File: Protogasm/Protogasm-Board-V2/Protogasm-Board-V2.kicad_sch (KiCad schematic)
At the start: 10 parts, among them J1 Neopixel_Ring_Header, M1 Motor_DC, Q1 FQP30N06L, SW1 Rotary_Encoder_Switch, U1 Arduino_UNO_R3, U2 MPX5050GP

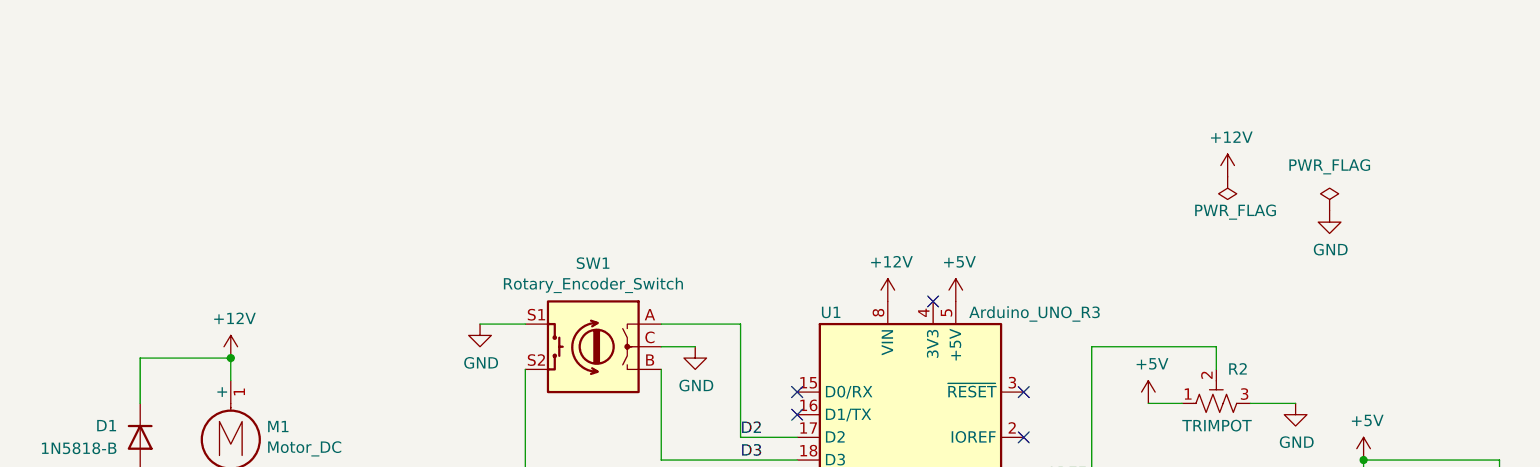
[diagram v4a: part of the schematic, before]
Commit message: Update schematic for V4
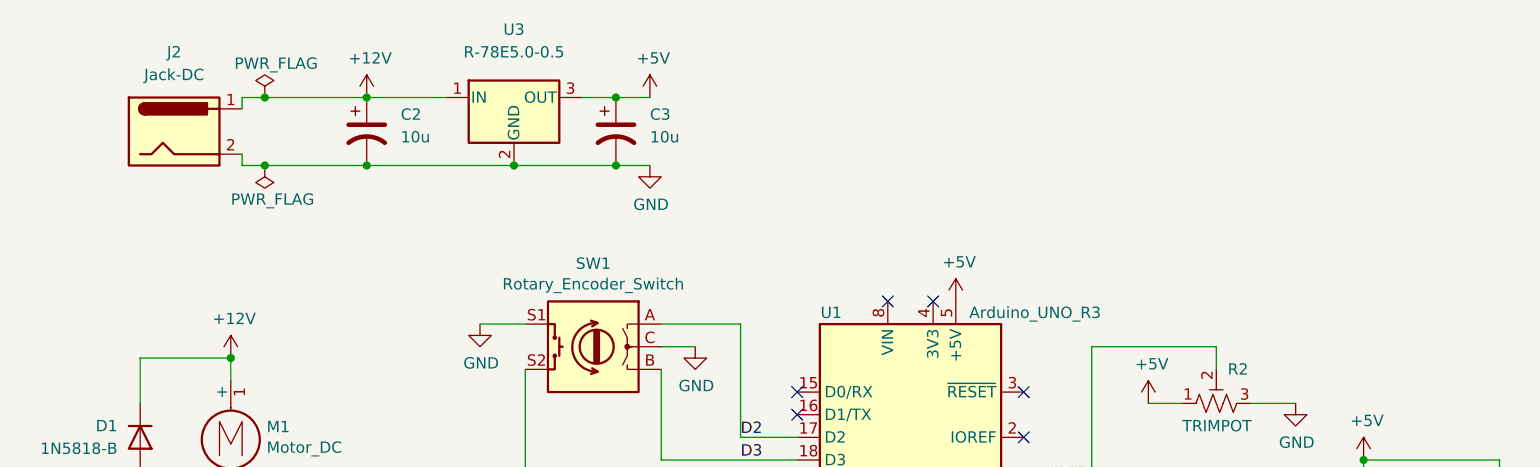
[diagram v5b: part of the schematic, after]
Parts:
- added C2, C3: 10u, Capacitor_THT:CP_Radial_D5.0mm_P2.50mm, symbol Device:C_Polarized_US
- added J2: Jack-DC, custom-footprints:2.1mm DC Barrel Jack, symbol Connector:Jack-DC
- added U3: R-78E5.0-0.5, Converter_DCDC:Converter_DCDC_RECOM_R-78E-0.5_THT, symbol Regulator_Switching:R-78E5.0-0.5
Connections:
- net +12V: now also C2.1, J2.1, U3.1 (IN); no longer U1.8 (VIN)
- net +5V: now also C3.1, U3.3 (OUT)
- net GND: now also C2.2, C3.2, J2.2, U3.2 (GND)
- no-connect marks 24 -> 25
